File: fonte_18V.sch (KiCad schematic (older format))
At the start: 15 parts

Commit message: update 2
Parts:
- removed D?: D, symbol Device:D
- removed J?: Screw_Terminal_01x02, symbol Connector:Screw_Terminal_01x02
- removed U?: LMR16030, symbol zenite_fonte:LMR16030
- added Cin2, Cout2: 100nF, Capacitor_SMD:C_0805_2012Metric_Pad1.15x1.40mm_HandSolder, symbol fonte_18V-rescue:C_Small-Device
- added D1: MBR20200CTG, Package_TO_SOT_THT:TO-220-3_Horizontal_TabDown_SMD, symbol fonte_18V-rescue:D_Schottky_AKA-Device
- added H1, H2, H3, H4: MountingHole, MountingHole:MountingHole_3mm, symbol Mechanical:MountingHole
- added Led1: LED, LED_SMD:LED_0805_2012Metric_Pad1.15x1.40mm_HandSolder, symbol fonte_18V-rescue:LED-Device
- added RLed1: 750R, Resistor_SMD:R_0805_2012Metric_Pad1.15x1.40mm_HandSolder, symbol fonte_18V-rescue:R_Small-Device
- added Rfbt2: 47k, Resistor_SMD:R_0805_2012Metric_Pad1.15x1.40mm_HandSolder, symbol fonte_18V-rescue:R_Small-Device
- added U1: LMR16030, symbol zenite_fonte:LMR16030
- CBoot1: renamed from C?; value C_Small -> 100nF; footprint (none) -> Capacitor_SMD:C_0805_2012Metric_Pad1.15x1.40mm_HandSolder; symbol Device:C_Small -> fonte_18V-rescue:C_Small-Device
- Cff1: renamed from C?; value C_Small -> 33.0pF; footprint (none) -> Capacitor_SMD:C_0805_2012Metric_Pad1.15x1.40mm_HandSolder; symbol Device:C_Small -> fonte_18V-rescue:C_Small-Device
- Cin1, Cout1: renamed from C?; value C_Small -> 100uF; footprint (none) -> Capacitor_THT:CP_Radial_D8.0mm_P3.80mm; symbol Device:C_Small -> fonte_18V-rescue:C_Small-Device
- D2: renamed from D?; value D -> SS35; footprint (none) -> Diode_SMD:D_SMC_Handsoldering; symbol Device:D -> fonte_18V-rescue:D-Device
- F1: renamed from F?; footprint (none) -> KicadZeniteSolarLibrary18:Fuse_Holder_5x20; symbol Device:Fuse -> fonte_18V-rescue:Fuse-Device
- L1: renamed from L?; value INDUCTOR -> 100uH; footprint (none) -> Inductor_THT:L_Radial_D21.0mm_P19.00mm; symbol pspice:INDUCTOR -> fonte_18V-rescue:INDUCTOR-pspice
- Q1: renamed from Q?; footprint (none) -> Package_TO_SOT_SMD:SOT-23_Handsoldering; symbol Device:Q_NMOS_GSD -> fonte_18V-rescue:Q_NMOS_GSD-Device
- R1: renamed from R?; value R_Small -> 47k; footprint (none) -> Resistor_SMD:R_0805_2012Metric_Pad1.15x1.40mm_HandSolder; symbol Device:R_Small -> fonte_18V-rescue:R_Small-Device
- Rfbb1: renamed from R?; value R_Small -> 2k2; footprint (none) -> Resistor_SMD:R_0805_2012Metric_Pad1.15x1.40mm_HandSolder; symbol Device:R_Small -> fonte_18V-rescue:R_Small-Device
- Rfbt1: renamed from R?; value R_Small -> 5k6; footprint (none) -> Resistor_SMD:R_0805_2012Metric_Pad1.15x1.40mm_HandSolder; symbol Device:R_Small -> fonte_18V-rescue:R_Small-Device
- battery1: renamed from BT?; value Battery -> 21.5<+VBAT<55V1; symbol Device:Battery -> fonte_18V-rescue:Battery-Device
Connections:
- wire segments 52 -> 73
- no-connect marks 0 -> 1

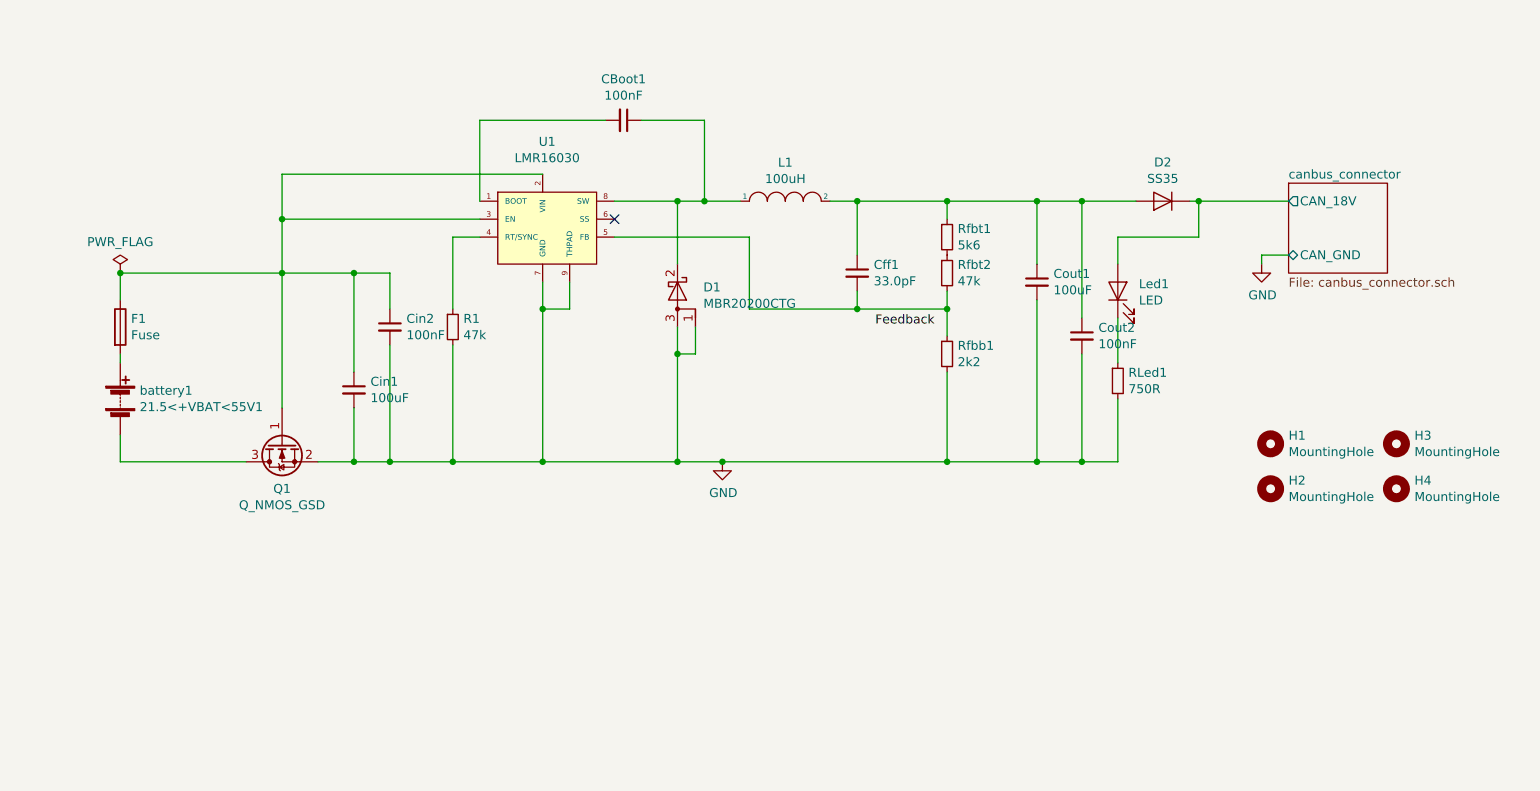
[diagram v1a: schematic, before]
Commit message: conectores e proteção de polaridade
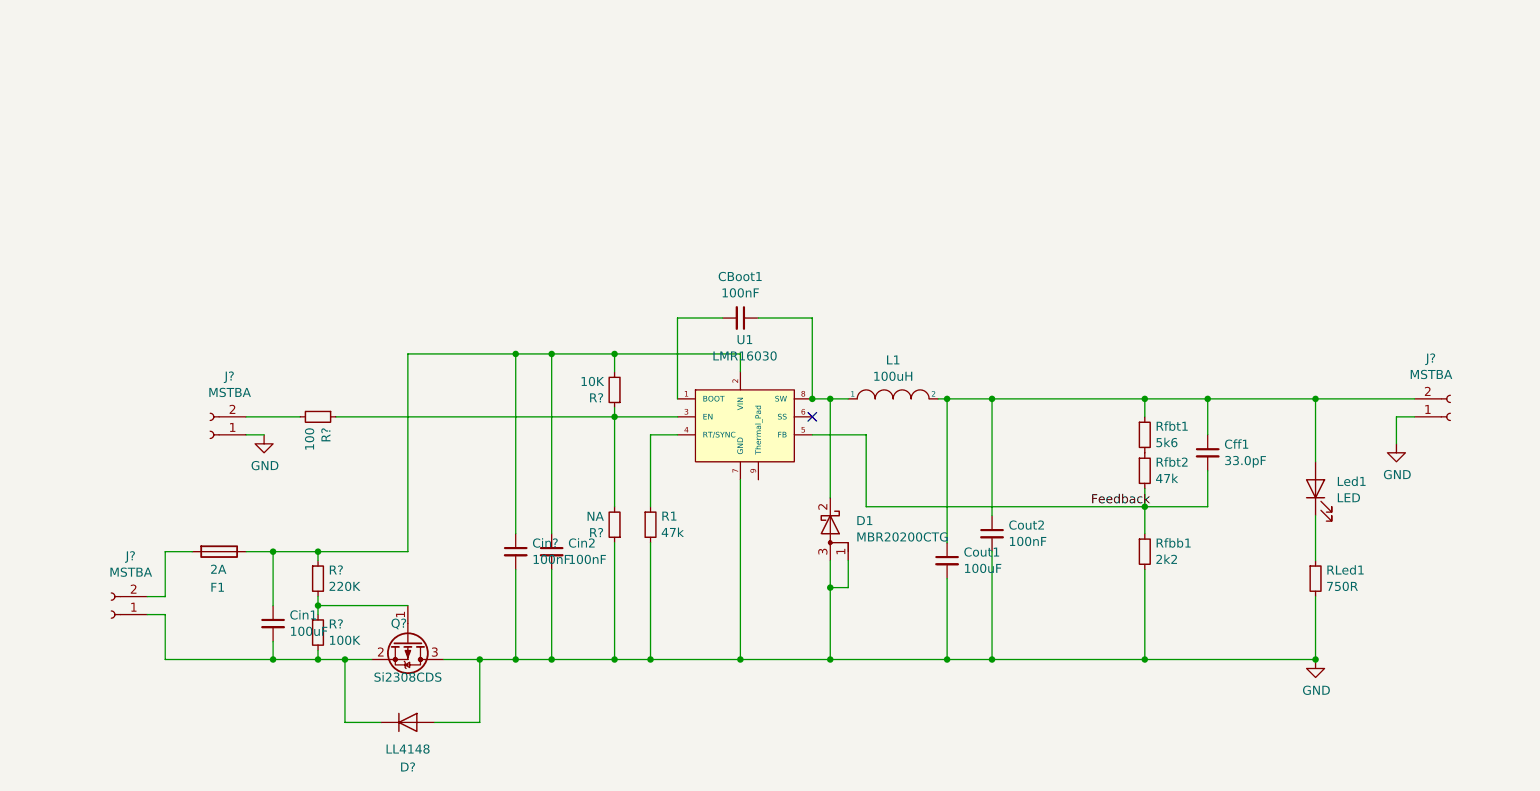
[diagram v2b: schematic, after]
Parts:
- removed D2: SS35, Diode_SMD:D_SMC_Handsoldering, symbol fonte_18V-rescue:D-Device
- removed H1, H2, H3, H4: MountingHole, MountingHole:MountingHole_3mm, symbol Mechanical:MountingHole
- removed Q1: Q_NMOS_GSD, Package_TO_SOT_SMD:SOT-23_Handsoldering, symbol fonte_18V-rescue:Q_NMOS_GSD-Device
- removed U1: LMR16030, symbol zenite_fonte:LMR16030
- removed battery1: 21.5<+VBAT<55V1, TerminalBlock:TerminalBlock_bornier-2_P5.08mm, symbol fonte_18V-rescue:Battery-Device
- added Cin?: 100nF, Capacitor_SMD:C_0805_2012Metric_Pad1.15x1.40mm_HandSolder, symbol fonte_18V-rescue:C_Small-Device
- added D?: LL4148, Diode_SMD:D_MiniMELF, symbol Diode:LL4148
- added J? (x3): MSTBA, Connector_Phoenix_MSTB:PhoenixContact_MSTBA_2,5_2-G-5,08_1x02_P5.08mm_Horizontal, symbol Connector:Conn_01x02_Female
- added Q?: Si2308CDS, Package_TO_SOT_SMD:SOT-23, symbol Transistor_FET:Si2319CDS
- added R?: 100, Resistor_SMD:R_0805_2012Metric_Pad1.15x1.40mm_HandSolder, symbol fonte_18V-rescue:R_Small-Device
- added R?: 10K, Resistor_SMD:R_0805_2012Metric_Pad1.15x1.40mm_HandSolder, symbol fonte_18V-rescue:R_Small-Device
- added R?: NA, Resistor_SMD:R_0805_2012Metric_Pad1.15x1.40mm_HandSolder, symbol fonte_18V-rescue:R_Small-Device
- added R?: 220K, Resistor_SMD:R_0805_2012Metric_Pad1.15x1.40mm_HandSolder, symbol fonte_18V-rescue:R_Small-Device
- added R?: 100K, Resistor_SMD:R_0805_2012Metric_Pad1.15x1.40mm_HandSolder, symbol fonte_18V-rescue:R_Small-Device
- added U1: LMR16030, Package_SO:Texas_R-PDSO-G8_EP2.95x4.9mm_Mask2.4x3.1mm_ThermalVias, symbol fonte_18V-rescue:LMR16030-zenite_fonte
- F1: value Fuse -> 2A
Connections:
- net canbus_connector/CAN_18V is gone; now on an unnamed net: Led1.2 (A)
- net Feedback: now also Cff1.2, Rfbb1.1, Rfbt2.2, U1.5 (FB)
- net GND: now also Cin?.2, D?.2 (A), J?.1 (Pin_1), J?.1 (Pin_1), Q?.3 (D), R?.1, U1.7 (GND); no longer Cin1.2
- net at Cin1.1, Cin2.1, F1.1: now also Cin?.1, R?.1, R?.2, U1.2 (VIN)
- net at R1.1: now also U1.4 (RT/SYNC)
- net at CBoot1.1, D1.2 (K), L1.1: now also U1.8 (SW)
- net at Cff1.1, Cout1.1, Cout2.1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: now also J?.2 (Pin_2)
- net at CBoot1.2: now also U1.1 (BOOT)
- net at F1.2: now also J?.2 (Pin_2)
- new net: Cin1.2, D?.1 (K), J?.1 (Pin_1), Q?.2 (S), R?.2
- new net: R?.1, R?.1, R?.2, U1.3 (EN)
- new net: Q?.1 (G), R?.1, R?.2
- new net: J?.2 (Pin_2), R?.2
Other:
- moved on the sheet: CBoot1, Cff1, Cin1, Cin2, Cout1, Cout2, D1, F1, L1, Led1, R1, RLed1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
